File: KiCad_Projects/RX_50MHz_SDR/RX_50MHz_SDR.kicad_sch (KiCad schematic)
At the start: 7 parts, among them Q1 SP010N70T8, U1 ESP32-S3, U2 Mixer, U3 LNA, U4 ESP32-S3-WROOM-1, U5 ADS1115IDGS, Y1 Si5351A-B-GM

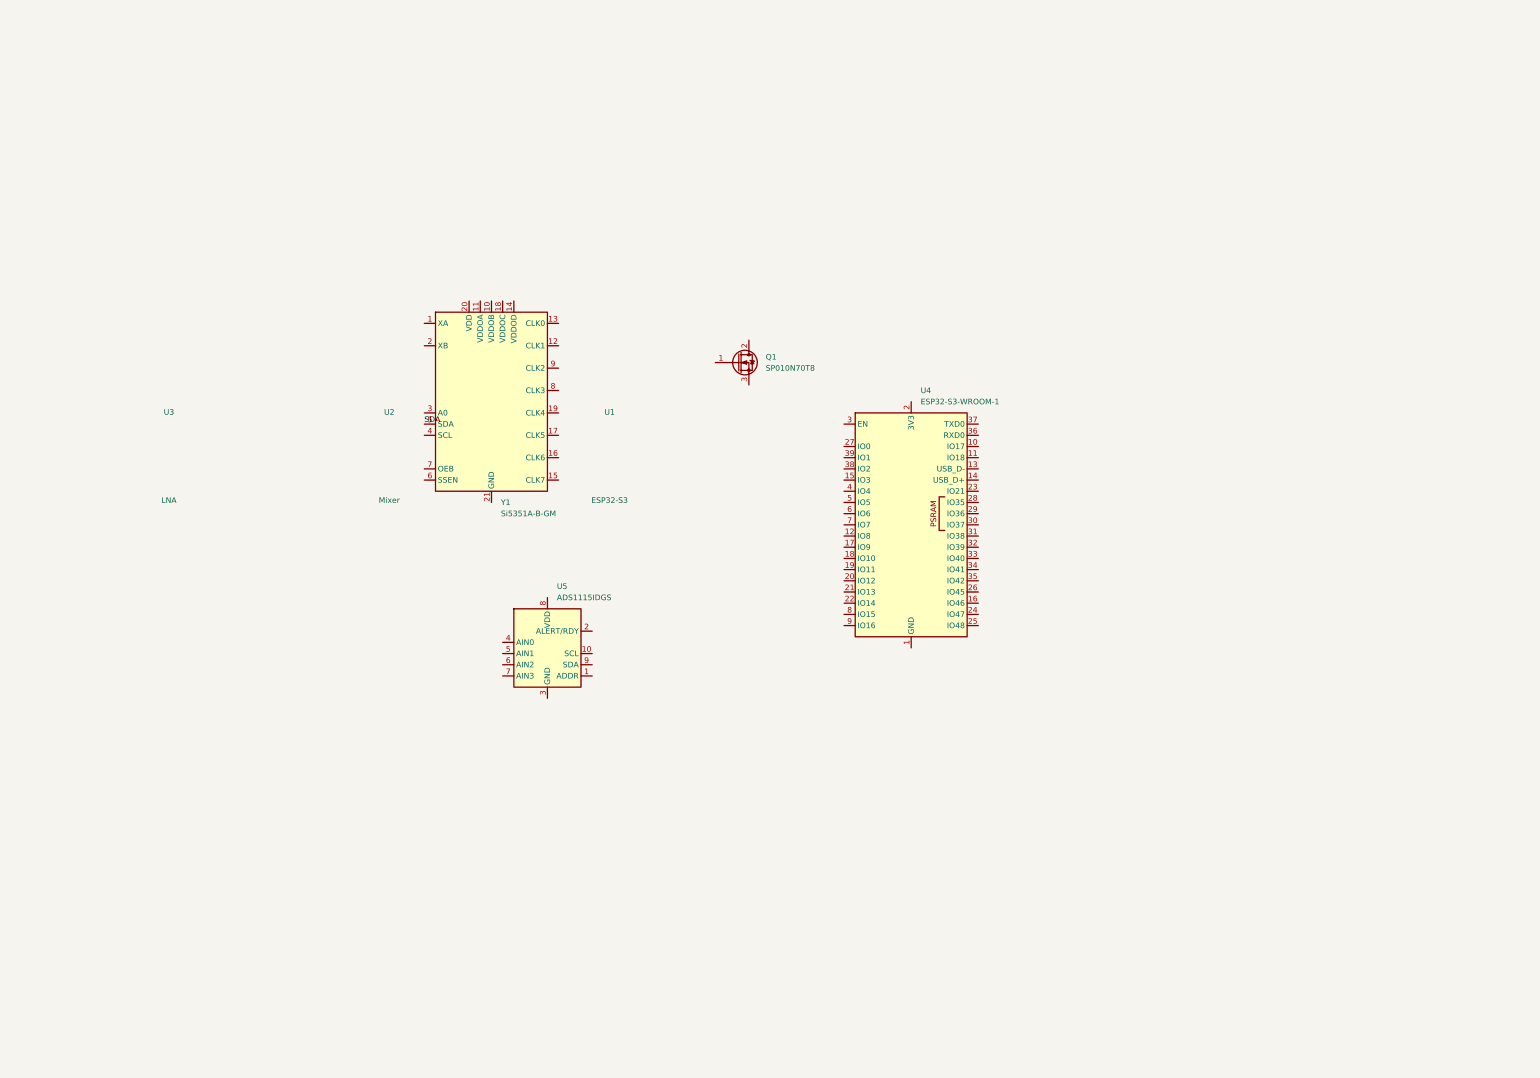
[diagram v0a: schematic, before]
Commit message: Sync TX and RX schematic connectivity with target netlists
Repair the electrical connectivity of both single-sheet schematics so that a
netlist exported with kicad-cli 10 matches the connectivity described by
TX_50MHz_1W.net / RX_50MHz_SDR.net and the TX/RX schematic blueprints.

TX_50MHz_1W.kicad_sch
- Split the I2C bus: two coincident global labels (I2C_SDA + I2C_SCL on the
  same point at ESP32 IO11) had merged SDA and SCL into one net that also
  dragged in the BGS12PL6 CTRL/RF2 pins and the SPF5043Z RF input.  SDA now
  lands on IO8 and SCL on IO9 only.
- Removed the wire chain that shorted ESP32 IO8..IO11 together.
- 3V3 rail: every IC VDD sat on an island with just its decoupling cap.
  Labelled U1/U2/U3/U6/U7/U8 supply pins onto 3V3, and grounded the six
  decoupling caps that had a floating leg.
- PA drain: dropped the junction that tied Q1 drain onto the Si5351A CLK1
  wire.  TX_PATH is now Q1 drain + BGS12PL6 RF1 + RFC L2, with V_BATT feeding
  the drain through L2 as the blueprint specifies.  TELEM_LO (CLK1 -> LT5560
  LO+) is carried by labels instead of a wire crossing the drain node.
- Telemetry RX chain: BGS12PL6 RF2 -> SPF5043Z RFin (RX_PATH) and SPF5043Z
  RFout -> LT5560 IN+ (LNA_OUT) were open (wires stopped short of the pin).
- ADC: the 10.7MHz filter output ran to a wire end 4.5mm away from the MCU.
  FL1 OUT and ESP32 IO10 are now on ADC_IN.
- T/R control: BGS12PL6 CTRL and ESP32 IO11 are now on TR_SW_CTRL.
- Output LPF: the four shunt caps had GND on their series legs, which shorted
  the BGS12PL6 antenna port and the whole filter to ground.  GND moved to the
  free leg of each cap and the series path is now a proper 4C/3L low-pass
  from the switch ANT pin to the SMA.

RX_50MHz_SDR.kicad_sch
- Si5351A VDD was held on 3V3 only by a label sitting mid-wire; moved it to
  the open end of the stub, matching the SCL/SDA stubs next to it.
- Removed the duplicate XTAL_A label (two identical labels on one point
  cancel each other out in KiCad, so th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
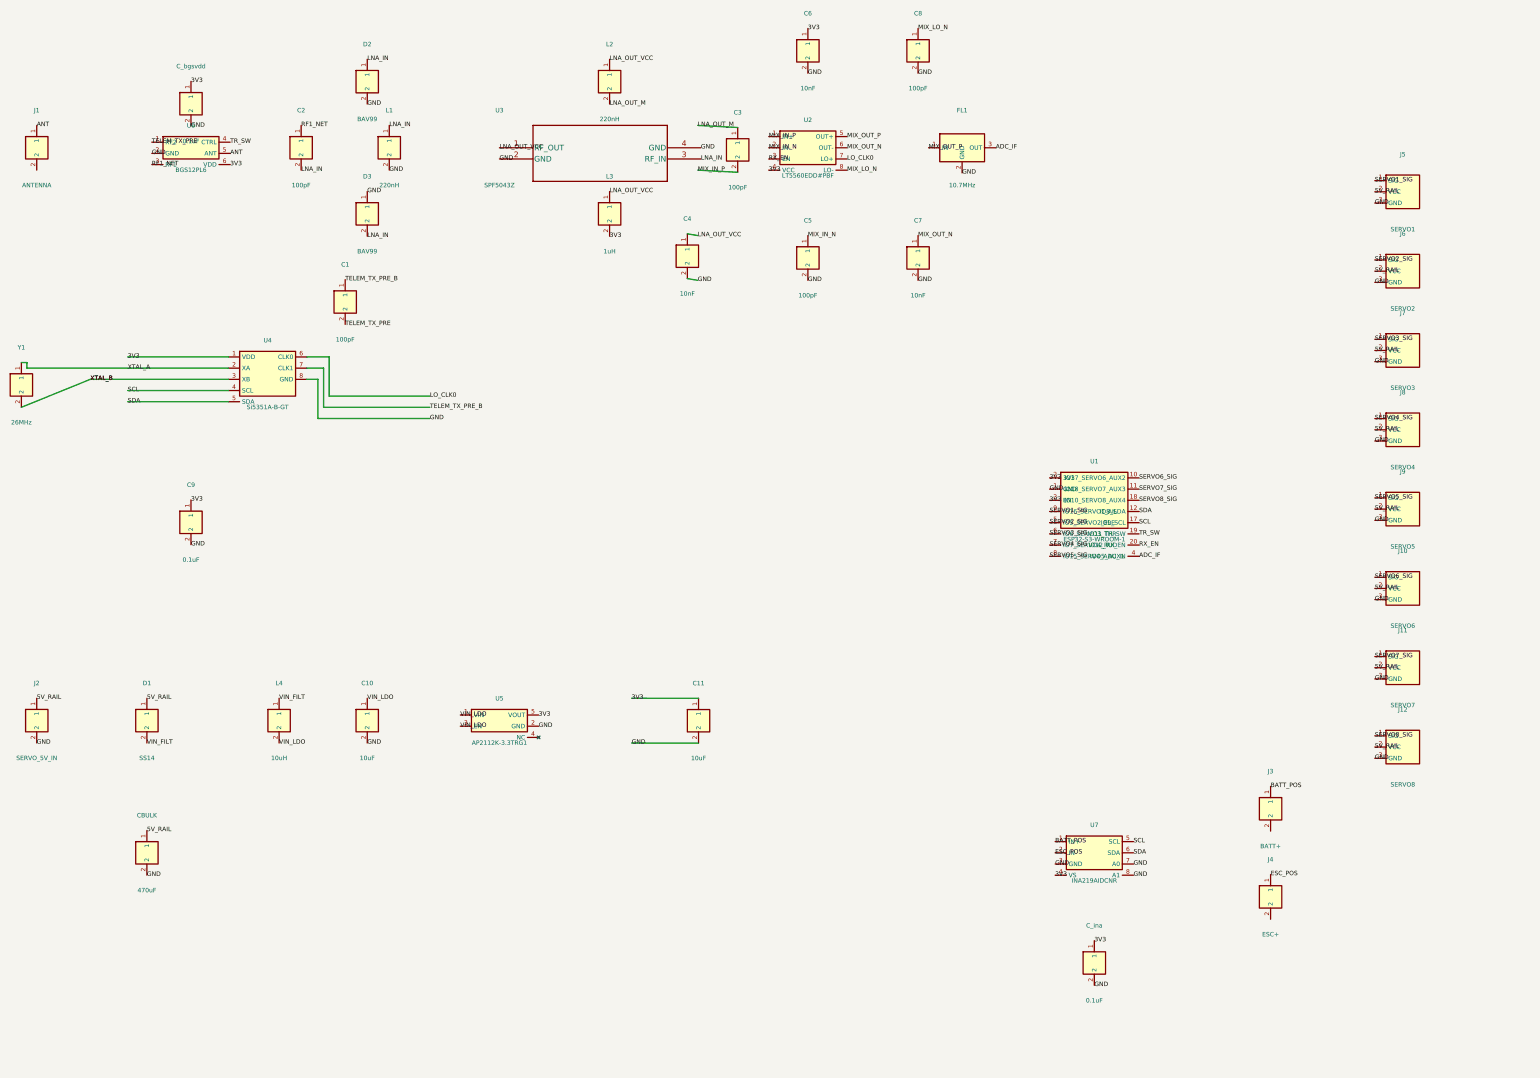
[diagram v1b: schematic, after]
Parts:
- removed Q1: SP010N70T8, Package_TO_SOT_SMD:SOT-89-3, symbol Transistor_FET_Other:SP010N70T8
- removed U1: ESP32-S3, symbol ESP32-S3-WROOM-1
- removed U2: Mixer, symbol LT5560
- removed U3: LNA, symbol SPF5043Z
- removed U4: ESP32-S3-WROOM-1, RF_Module:ESP32-S3-WROOM-1, symbol RF_Module:ESP32-S3-WROOM-1
- removed U5: ADS1115IDGS, Package_SO:TSSOP-10_3x3mm_P0.5mm, symbol Analog_ADC:ADS1115IDGS
- removed Y1: Si5351A-B-GM, Package_DFN_QFN:QFN-20-1EP_4x4mm_P0.5mm_EP2.7x2.7mm, symbol Oscillator:Si5351A-B-GM
- added C1, C2, C3, C5, C8: 100pF, Capacitor_SMD:C_0603_1608Metric, symbol Custom:CAP
- added C10, C11: 10uF, Capacitor_SMD:C_0805_2012Metric, symbol Custom:CAP
- added C4, C6, C7: 10nF, Capacitor_SMD:C_0603_1608Metric, symbol Custom:CAP
- added C9, C_bgsvdd, C_ina: 0.1uF, Capacitor_SMD:C_0603_1608Metric, symbol Custom:CAP
- added CBULK: 470uF, CP_Elec_8x10.5, symbol Custom:CAP
- added D1: SS14, Diode_SMD:D_SMA, symbol Custom:DIODE
- added D2, D3: BAV99, Package_TO_SOT_SMD:SOT-23, symbol Custom:DIODE
- added FL1: 10.7MHz, Filter:Filter_Murata_SFECF-6, symbol Custom:FILTER3
- added J1: ANTENNA, Connector:U.FL_Vertical, symbol Custom:HDR1
- added J10: SERVO6, Connector_PinHeader_2.54mm:PinHeader_1x03_P2.54mm_Vertical, symbol Custom:HDR3
- added J11: SERVO7, Connector_PinHeader_2.54mm:PinHeader_1x03_P2.54mm_Vertical, symbol Custom:HDR3
- added J12: SERVO8, Connector_PinHeader_2.54mm:PinHeader_1x03_P2.54mm_Vertical, symbol Custom:HDR3
- added J2: SERVO_5V_IN, Connector_PinHeader_2.54mm:PinHeader_1x02_P2.54mm_Vertical, symbol Custom:HDR1
- added J3: BATT+, Connector_PinHeader_2.54mm:PinHeader_1x01_P2.54mm_Vertical, symbol Custom:HDR1
- added J4: ESC+, Connector_PinHeader_2.54mm:PinHeader_1x01_P2.54mm_Vertical, symbol Custom:HDR1
- added J5: SERVO1, Connector_PinHeader_2.54mm:PinHeader_1x03_P2.54mm_Vertical, symbol Custom:HDR3
- added J6: SERVO2, Connector_PinHeader_2.54mm:PinHeader_1x03_P2.54mm_Vertical, symbol Custom:HDR3
- added J7: SERVO3, Connector_PinHeader_2.54mm:PinHeader_1x03_P2.54mm_Vertical, symbol Custom:HDR3
- added J8: SERVO4, Connector_PinHeader_2.54mm:PinHeader_1x03_P2.54mm_Vertical, symbol Custom:HDR3
- added J9: SERVO5, Connector_PinHeader_2.54mm:PinHeader_1x03_P2.54mm_Vertical, symbol Custom:HDR3
- added L1, L2: 220nH, Inductor_SMD:L_0603_1608Metric, symbol Custom:IND
- added L3: 1uH, Inductor_SMD:L_0805_2012Metric, symbol Custom:IND
- added L4: 10uH, Inductor_SMD:L_0805_2012Metric, symbol Custom:IND
- added U1: ESP32-S3-WROOM-1, RF_Module:ESP32-S3-WROOM-1-N16R8, symbol Custom:ESP32S3
- added U2: LT5560EDD#PBF, Package_DFN_QFN:DFN-8-1EP_3x3mm_P0.5mm, symbol Custom:LT5560
- added U3: SPF5043Z, SPF5043Z_QOR, symbol Custom:SPF5043Z
- added U4: Si5351A-B-GT, Package_SO:MSOP-10_3x3mm_P0.5mm, symbol Custom:SI5351A
- added U5: AP2112K-3.3TRG1, Package_TO_SOT_SMD:SOT-23-5, symbol Custom:AP2112K
- added U6: BGS12PL6, Package_SON:TSLP-6-4_0.7x1.1mm_P0.4mm, symbol Custom:BGS12PL6
- added U7: INA219AIDCNR, Package_TO_SOT_SMD:SOT-23-8, symbol Custom:INA219
- added Y1: 26MHz, Crystal:Crystal_SMD_3225-4Pin_3.2x2.5mm, symbol Custom:XTAL
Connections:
- net SDA: now also U1.12 (IO8_SDA), U4.5 (SDA), U7.6 (SDA)
- new net 3V3: C11.1, C6.1, C9.1, C_bgsvdd.1, C_ina.1, L3.2, U1.2 (3V3), U1.3 (EN), U2.4 (VCC), U4.1 (VDD), U5.5 (VOUT), U6.6 (VDD), U7.4 (VS)
- new net 5V_RAIL: CBULK.1, D1.1, J10.2 (VCC), J11.2 (VCC), J12.2 (VCC), J2.1, J5.2 (VCC), J6.2 (VCC), J7.2 (VCC), J8.2 (VCC), J9.2 (VCC)
- new net ADC_IF: FL1.3 (OUT), U1.4 (IO4_ADC_IN)
- new net ANT: J1.1, U6.5 (ANT)
- new net BATT_POS: J3.1, U7.1 (IN+)
- new net ESC_POS: J4.1, U7.2 (IN-)
- new net GND: C10.2, C11.2, C4.2, C5.2, C6.2, C7.2, C8.2, C9.2, CBULK.2, C_bgsvdd.2, C_ina.2, D2.2, D3.1, FL1.2 (GND), J10.3 (GND), J11.3 (GND), J12.3 (GND), J2.2, J5.3 (GND), J6.3 (GND), J7.3 (GND), J8.3 (GND), J9.3 (GND), L1.2, U1.1 (GND), U3.2 (GND), U3.4 (GND), U4.8 (GND), U5.2 (GND), U6.2 (GND), U7.3 (GND), U7.7 (A0), U7.8 (A1)
- new net LNA_IN: C2.2, D2.1, D3.2, L1.1, U3.3 (RF_IN)
- new net LNA_OUT_M: C3.1, L2.2
- new net LNA_OUT_VCC: C4.1, L2.1, L3.1, U3.1 (RF_OUT)
- new net LO_CLK0: U2.7 (LO+), U4.6 (CLK0)
- new net MIX_IN_N: C5.1, U2.2 (IN-)
- new net MIX_IN_P: C3.2, U2.1 (IN+)
- new net MIX_LO_N: C8.1, U2.8 (LO-)
- new net MIX_OUT_N: C7.1, U2.6 (OUT-)
- new net MIX_OUT_P: FL1.1 (IN), U2.5 (OUT+)
- new net RF1_NET: C2.1, U6.3 (RF1)
- new net RX_EN: U1.20 (IO12_RX_EN), U2.3 (EN)
- new net SCL: U1.17 (IO9_SCL), U4.4 (SCL), U7.5 (SCL)
- new net SERVO1_SIG: J5.1 (SIG), U1.9 (IO16_SERVO1_AIL)
- new net SERVO2_SIG: J6.1 (SIG), U1.5 (IO5_SERVO2_ELE)
- new net SERVO3_SIG: J7.1 (SIG), U1.6 (IO6_SERVO3_THR)
- new net SERVO4_SIG: J8.1 (SIG), U1.7 (IO7_SERVO4_RUD)
- new net SERVO5_SIG: J9.1 (SIG), U1.8 (IO15_SERVO5_AUX1)
- new net SERVO6_SIG: J10.1 (SIG), U1.10 (IO17_SERVO6_AUX2)
- new net SERVO7_SIG: J11.1 (SIG), U1.11 (IO18_SERVO7_AUX3)
- new net SERVO8_SIG: J12.1 (SIG), U1.18 (IO10_SERVO8_AUX4)
- new net TELEM_TX_PRE: C1.2, U6.1 (RF2)
- new net TELEM_TX_PRE_B: C1.1, U4.7 (CLK1)
- new net TR_SW: U1.19 (IO11_TR_SW), U6.4 (CTRL)
- new net VIN_FILT: D1.2, L4.1
- new net VIN_LDO: C10.1, L4.2, U5.1 (VIN), U5.3 (EN)
- new net XTAL_A: U4.2 (XA), Y1.1
- new net XTAL_B: U4.3 (XB), Y1.2
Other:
- title: (none) -> 50MHz RC Receiver - Auto-Generated Schematic

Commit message: Lay out TX and RX schematics for readability (cosmetic only)
Both sheets had all content crammed into the top-left corner with
overlapping connector labels. Repositioned symbols into functional
bands with generous spacing:

TX (A3): three bands - TX RF chain (crystal -> Si5351 synth -> RD01MUS2
PA -> BGS12PL6 T/R switch -> 7-element LPF ladder -> ANT) across the
top with the LPF laid out as one straight line; RX down-conversion
chain plus OLED/I2C in the middle; ESP32, both ADS1115 + stick blocks
and the remaining stick/aux/power headers along the bottom. J1-J7 were
clipping the left page edge at x=2mm; now inset with real vertical
pitch between entries.

RX: page reduced A2 -> A3 (A2 was ~4x oversized for the content), then
five bands - RF signal path, RF support (clamps/bias/decoupling placed
under the IC each one serves), LO + ESP32 + servo outputs, 5V->3V3
power chain, and bulk cap + INA219 telemetry. Servo headers J5-J12
regrouped from one 18mm-pitch column (labels collided) into two
columns of four at 31mm pitch.

Connectivity is unchanged: symbols were translated only as whole rigid
groups (symbol plus every wire/label coincident with its pins), and
netlists exported before and after with kicad-cli compare as an
identical partition of (ref,pin) pairs into nets - TX 36 nets / 132
pins, RX 39 nets / 134 pins. No net, symbol, value or property was
added, removed or changed; the diff touches only coordinate values
plus RX's paper size.

Co-Authored-By: Claude Sonnet 5 <noreply@anthropic.com>
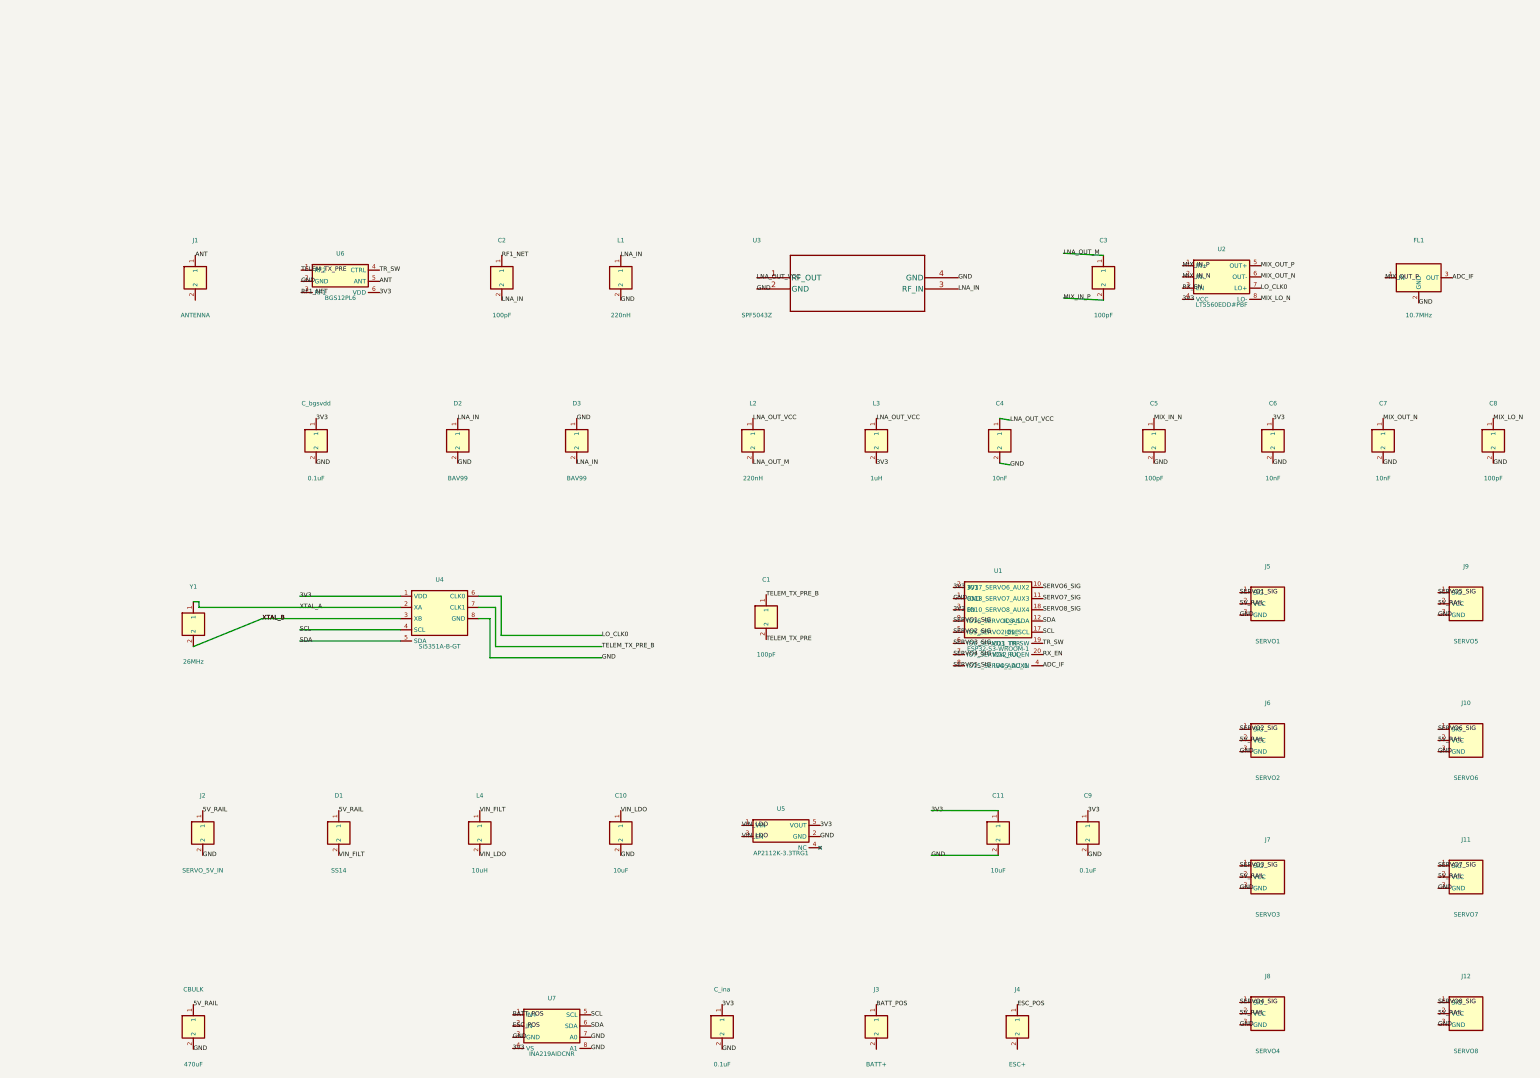
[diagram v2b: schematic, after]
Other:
- moved on the sheet: C1, C10, C11, C2, C3, C4, C5, C6, C7, C8, C9, CBULK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
